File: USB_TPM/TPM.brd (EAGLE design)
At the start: 45 x 19 mm, 47 parts, among them U1 SAM4S4A, X1 TC2050-NL-MCP-NL, Y1 12MHZ

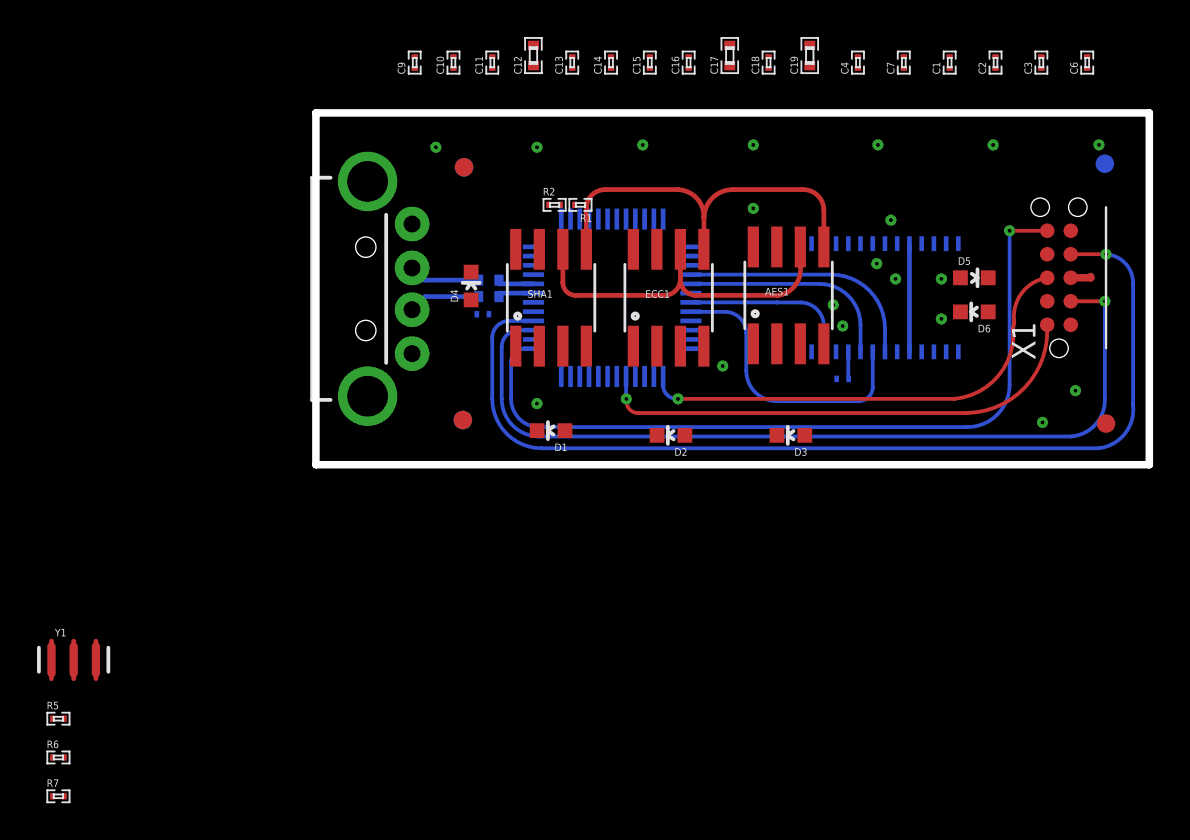
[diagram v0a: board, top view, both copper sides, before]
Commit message: schematic complete, board has 57 airwires
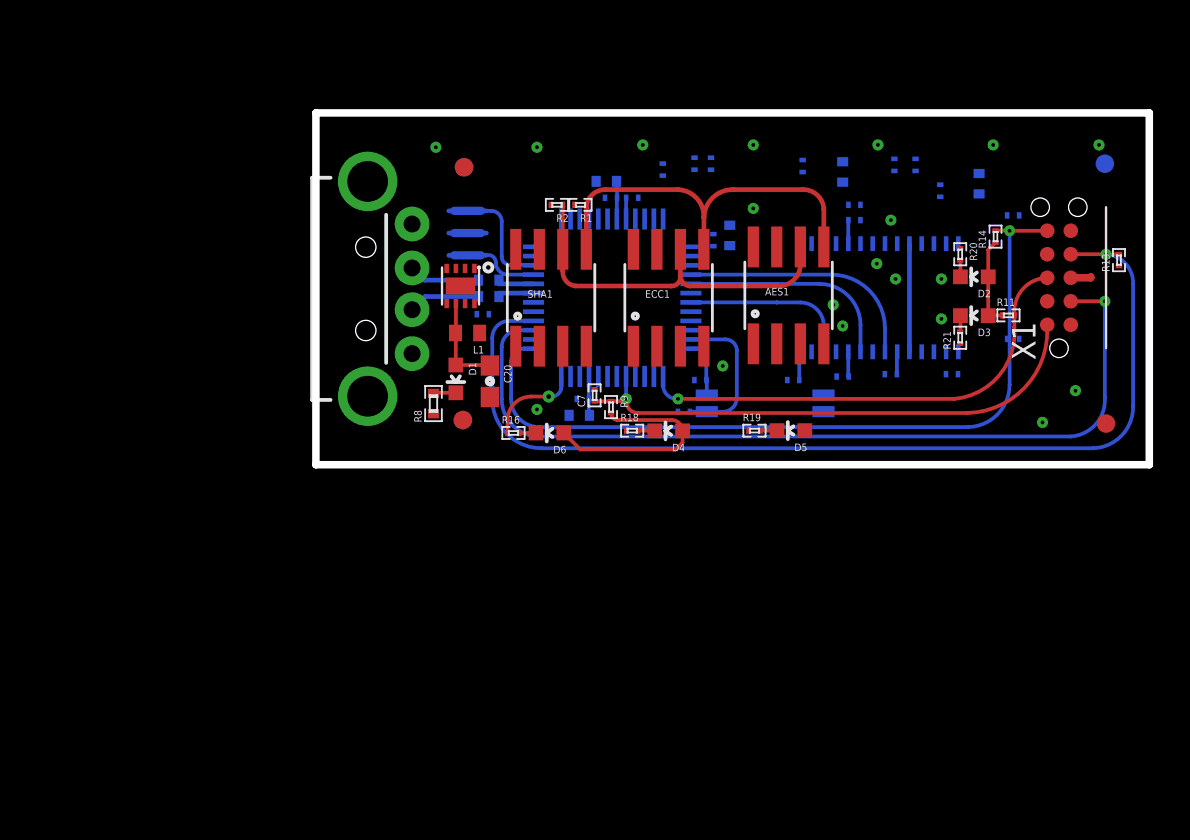
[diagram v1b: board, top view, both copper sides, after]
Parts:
- removed FRAME1: FRAME-LEDGER, TPM:CREATIVE_COMMONS
- added C20: 22uF, TPM:0603
- added C21: 2.2uF, TPM:0201
- added C22: 10uF, TPM:0402
- added C23, C24, R16, R18, R19, R20, R21: (no value), TPM:0201
- added L1: 2.2uH, TPM:C0402
- added R10: 4.7, TPM:0402
- added R11, R12, R13, R14, R15, R9: 100K, TPM:0201
- added R8: 470, TPM:0402
- added U2: TPS62172, TPM:WSON-8-PAD
- added Y2: (no value), TPM:CRYSTAL-32KHZ-SMD_EPSON_MC146
- C1, C3: value 2200pF -> 0.1uF
- C7: value 2200pF -> (none)
- R1: value 2.2K -> 825
- R2: value 2.2K -> 3.92K
- R6: value (none) -> 4.7K
- R7: value (none) -> 10K
- moved R7 53.4 mm to (34.4, 4.89), flipped to the bottom
- moved R6 49.5 mm to (31.1, 4.89), flipped to the bottom
- moved R5 43.7 mm to (25.8, 4.57), flipped to the bottom
- moved Y1 31.4 mm to (8.19, 12.5), flipped to the bottom, turned to 90 degrees
- moved C7 24.5 mm to (15.0, 3.75)
- moved D6 23.8 mm to (12.6, 1.71)
- moved C17 21.1 mm to (14.2, 2.67), flipped to the bottom, turned to 0 degrees
- moved C16 19.0 mm to (14.4, 3.56), flipped to the bottom, turned to 0 degrees
- moved D2 18.5 mm to (35.6, 10.1)
- moved D4 13.2 mm to (19.1, 1.83), turned to 90 degrees
- moved D5 12.9 mm to (25.7, 1.84), turned to 90 degrees
- moved C9 12.9 mm to (15.9, 14.4), flipped to the bottom, turned to 0 degrees
- moved C10 12.7 mm to (18.7, 15.9), flipped to the bottom
- moved D3 11.8 mm to (35.6, 8.05)
- moved C2 10.8 mm to (29.1, 14.0), flipped to the bottom, turned to 0 degrees
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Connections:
- removed net GPIO-EXPRESS-00: TPM1.6
- removed net N$7: U1.29, X1.10
- new net AES: R19.1, U1.35
- new net ECC: R18.1, U1.32
- new net N$16: D4.C, R18.2
- new net N$17: L1.1, U2.7
- new net N$18: D1.C, R8.2
- new net N$20: D6.C, R16.2
- new net N$21: D5.C, R19.2
- new net N$22: D2.C, R20.2
- new net N$23: D3.C, R21.2
- new net SHA: R16.1, U1.36
- new net STAT0: R20.1, U1.3
- new net STAT1: R21.1, U1.4
- new net VUSB: C21.1, C22.1, R10.2, U2.2, U2.3
- new net XIN32: C23.1, U1.24, Y2.P$1
- new net XOUT32: C24.1, U1.23, Y2.P$2
- net 3.3V: now also C20.1, D1.A, D2.A, D3.A, D4.A, D5.A, D6.A, L1.2, R11.1, R12.1, R13.1, R14.1, R15.2, R9.2, TPM1.5, U2.6; no longer C7.2
- net CS: now also R15.1
- net GND: now also C20.2, C21.2, C22.2, C23.2, C24.2, C7.2, R8.1, U2.1, U2.4, U2.5, U2.PAD; no longer C7.1
- net N$13: now also R10.1
- net N$15: now also TPM1.6
- net N$3: now also R11.2
- net N$4: now also R14.2
- net N$5: now also R12.2
- net N$6: now also R13.2
- net RST: now also C7.1, R9.1, U1.29, X1.10
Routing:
- net RST: track 0.00 -> 28.4 mm, vias 0 -> 1
- net 3.3V: track 7.34 -> 34.5 mm
- net N$7: track 26.6 -> 0.00 mm, vias 1 -> 0
- net CS: track 15.2 -> 0.00 mm
- net XOUT32: track 0.00 -> 8.12 mm
- net SHA: track 0.00 -> 4.91 mm, vias 0 -> 1
- net N$9: track 0.00 -> 4.88 mm
- net XIN32: track 0.00 -> 2.98 mm
- net N$8: track 0.00 -> 2.95 mm
- net N$15: track 0.00 -> 1.53 mm
- net N$18: track 0.00 -> 1.22 mm
- net N$10: track 0.00 -> 1.21 mm
- net 1.2V: track 0.00 -> 1.15 mm
- net SCL: track 19.1 -> 20.2 mm
- net N$22: track 0.00 -> 0.90 mm
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
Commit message: initial github commit
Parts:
- removed C15: .1uF, TPM:0201
- removed C21: 2.2uF, TPM:0201
- C23, C24: value (none) -> 22pF
- C5: value (none) -> 0.1uF
- C7: value (none) -> 0.02uF
- R16, R18, R19, R20, R21: value (none) -> 470
- R3, R4: value 27 Ohm -> 27
- R5: value (none) -> 4.7K
- Y2: value (none) -> 32KHz
- moved R10 27.3 mm to (8.57, 13.6), flipped to the top, turned to 180 degrees
- moved C22 21.3 mm to (7.49, 11.9), flipped to the top, turned to 180 degrees
- moved C14 9.49 mm to (11.6, 12.8)
- moved R15 7.84 mm to (30.0, 4.95), turned to 270 degrees
- moved R12 7.56 mm to (43.3, 8.48), flipped to the top, turned to 90 degrees
- moved C4 6.85 mm to (32.5, 13.3)
- moved C6 5.64 mm to (27.1, 14.2), turned to 180 degrees
- moved C10 5.16 mm to (22.1, 12.1)
- moved C3 5.03 mm to (27.1, 13.3), turned to 180 degrees
- moved C18 1.57 mm to (20.1, 12.9)
- moved C19 1.44 mm to (21.1, 13.1)
- moved C5 0.84 mm to (9.84, 8.26)
- moved R13 0.66 mm to (43.3, 11.7), turned to 270 degrees
- moved R3 0.46 mm to (8.88, 9.97)
- moved R4 0.46 mm to (8.88, 9.08)
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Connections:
- net 1.2V: no longer C15.1
- net GND: no longer C15.2, C21.2
- net SCL: now also U1.28
- net SDA: now also U1.31
- net VUSB: no longer C21.1
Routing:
- net STAT1: track 0.00 -> 34.9 mm, vias 0 -> 2
- net 3.3V: track 34.5 -> 67.7 mm, vias 0 -> 16
- net STAT0: track 0.00 -> 27.9 mm, vias 0 -> 2
- net 1.2V: track 1.15 -> 23.8 mm
- net AES: track 0.00 -> 16.4 mm, vias 0 -> 2
- net N$15: track 1.53 -> 16.7 mm, vias 0 -> 3
- net N$13: track 0.00 -> 13.2 mm, vias 0 -> 1
- net CS: track 0.00 -> 12.5 mm, vias 0 -> 2
- net ECC: track 0.00 -> 9.37 mm, vias 0 -> 1
- net SDA: track 21.1 -> 29.9 mm, vias 0 -> 1
- net RST: track 28.4 -> 36.2 mm, vias 1 -> 3
- net SCL: track 20.2 -> 25.9 mm, vias 0 -> 1
- net VUSB: track 0.00 -> 3.50 mm
- net N$17: track 0.00 -> 2.10 mm
- net N$14: track 0.00 -> 1.21 mm
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- added copper zone on layer 2, net 3.3V
- added copper zone on layer 15, net GND
